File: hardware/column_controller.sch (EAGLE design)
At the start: 35 parts, among them J4 JTAG, U1 ESP-WROVER-32ESP-WROVER-32, U2 3.3V, U3 CP2102N

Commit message: CAM
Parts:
- added FD1, FD2, FD3, FD4: FIDUCIAL1X2, SparkFun-Aesthetics:FIDUCIAL1X2
- added H1, H2, H3, H4: STAND-OFF, SparkFun-Hardware:STAND-OFF
- added R10, R11: 5.1k, SparkFun-Resistors:5.1KOHM5.1KOHM-0603-1/10W-1%
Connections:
- new net N$10: J3.CC1, R11.2
- new net N$11: J3.CC2, R10.2
- new net SHLD: J3.SHLD
- net 13: no longer R9.2
- net 3.3V: now also R9.2
- net GND: now also J3.GND, R10.1, R11.1

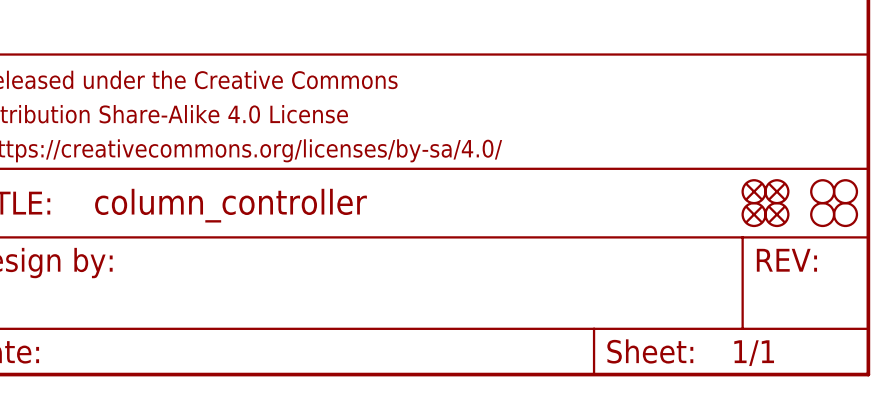
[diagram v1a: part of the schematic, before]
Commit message: bump column controller to v03
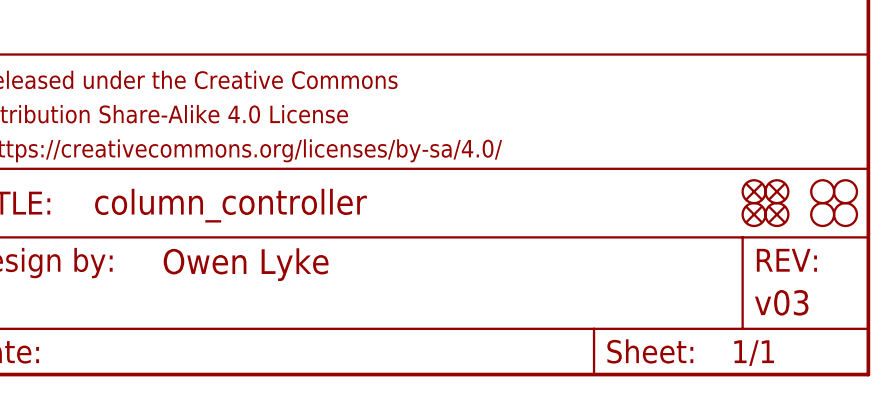
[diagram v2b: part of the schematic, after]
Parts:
- FRAME1: DESIGNER (none) -> Owen Lyke; REV (none) -> v03
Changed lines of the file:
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@@
 </classes>
 <parts>
-<part name="FRAME1" library="SparkFun-Aesthetics" deviceset="FRAME-LEDGER" device=""/>
+<part name="FRAME1" library="SparkFun-Aesthetics" deviceset="FRAME-LEDGER" device="">
+<attribute name="DESIGNER" value="Owen Lyke"/>
+<attribute name="REV" value="v03"/>
+</part>
 <part name="U1" library="SparkFun-RF" deviceset="ESP-WROVER-32" device="ESP-WROVER-32"/>
 <part name="SUPPLY1" library="SparkFun-PowerSymbols" deviceset="3.3V" device=""/>
